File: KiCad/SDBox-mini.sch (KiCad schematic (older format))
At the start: 25 parts, among them J1 DB25_Male, J2 Conn_02x03_Odd_Even, J3 Micro_SD_Card, J4 USB_B_Micro, U1 LM1117-3.3, U2 ATmega328P-AU, U3 74LVC3G17, U4 74LVC1G17, Y1 Crystal_GND24_Small

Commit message: adapted TSSOP-8_3x3mm_P0.65mm footprint for Handsoldering
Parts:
- U3: footprint Package_SO:TSSOP-8_3x3mm_P0.65mm -> SDBox-mini:TSSOP-8_3x3mm_P0.65mm_Custom_Handsoldering
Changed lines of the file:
@@
 F 0 "U3" H 6950 4915 50  0000 C CNN
 F 1 "74LVC3G17" H 6950 4824 50  0000 C CNN
-F 2 "Package_SO:TSSOP-8_3x3mm_P0.65mm" H 7800 4400 50  0001 C CNN
+F 2 "SDBox-mini:TSSOP-8_3x3mm_P0.65mm_Custom_Handsoldering" H 7800 4400 50  0001 C CNN
 F 3 "https://assets.nexperia.com/documents/data-sheet/74LVC3G17.pdf" H 7800 4400 50  0001 C CNN
 	1    6950 4000

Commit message: added optional pull-up on MOSI, fixed keep-out area of copper pour on U3,U4 GND-pads to neighbouring pad
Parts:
- added R6: 10k, Resistor_SMD:R_0603_1608Metric_Pad1.05x0.95mm_HandSolder, symbol Device:R_Small
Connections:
- net +5V: now also R6.2
- net MOSI: now also R6.1
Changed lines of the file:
@@
 Text GLabel 7900 2050 2    50   Input ~ 0
 3V3
-Text GLabel 6550 3450 0    50   Input ~ 0
+Text GLabel 6150 3450 0    50   Input ~ 0
 MOSI
 NoConn ~ 7900 1650
@@
 Wire Wire Line
 	10300 3300 10100 3300
+$Comp
+L Device:R_Small R6
+U 1 1 612033E9
+P 6350 3350
+F 0 "R6" H 6291 3304 50  0000 R CNN
+F 1 "10k" H 6291 3395 50  0000 R CNN
+F 2 "Resistor_SMD:R_0603_1608Metric_Pad1.05x0.95mm_HandSolder" H 6350 3350 50  0001 C CNN
+F 3 "~" H 6350 3350 50  0001 C CNN
+	1    6350 3350
+	-1   0    0    1
+$EndComp
+Text GLabel 6350 3250 1    50   Input ~ 0
+VCC
+Wire Wire Line
+	6350 3450 6550 3450
+Wire Wire Line
+	6150 3450 6350 3450
+Connection ~ 6350 3450
 $EndSCHEMATC

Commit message: added common pull-up for DAT1,DAT2-lines (pin 8 and 1) on MicroSD-connector-pads
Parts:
- added R5: 10k, Resistor_SMD:R_0603_1608Metric_Pad1.05x0.95mm_HandSolder, symbol Device:R_Small
- renumbered R5 to R7
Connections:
- net 3V3: now also R5.2
- net at J3.1 (NC): now also J3.8 (NC), R5.1
- no-connect marks 16 -> 14
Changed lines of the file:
@@
 	3950 1300 4050 1300
 $Comp
-L Device:R_Small R5
+L Device:R_Small R7
 U 1 1 60F84B00
 P 4950 2900
-F 0 "R5" H 4891 2854 50  0000 R CNN
+F 0 "R7" H 4891 2854 50  0000 R CNN
 F 1 "10k" H 4891 2945 50  0000 R CNN
 F 2 "Resistor_SMD:R_0603_1608Metric_Pad1.05x0.95mm_HandSolder" H 4950 2900 50  0001 C CNN
@@
 Text GLabel 4950 3100 2    50   Input ~ 0
 RESET
-NoConn ~ 7900 2350
 Text GLabel 10100 3700 2    50   Output ~ 0
 MISO
@@
 Text GLabel 6150 3450 0    50   Input ~ 0
 MOSI
-NoConn ~ 7900 1650
 Text GLabel 7900 2250 2    50   Input ~ 0
 CS
@@
 	6150 3450 6350 3450
 Connection ~ 6350 3450
+$Comp
+L Device:R_Small R5
+U 1 1 612155E1
+P 8500 1850
+F 0 "R5" H 8441 1804 50  0000 R CNN
+F 1 "10k" H 8441 1895 50  0000 R CNN
+F 2 "Resistor_SMD:R_0603_1608Metric_Pad1.05x0.95mm_HandSolder" H 8500 1850 50  0001 C CNN
+F 3 "~" H 8500 1850 50  0001 C CNN
+	1    8500 1850
+	-1   0    0    1
+$EndComp
+Text GLabel 8500 1750 1    50   Input ~ 0
+3V3
+Wire Wire Line
+	7900 1650 8400 1650
+Wire Wire Line
+	8400 1650 8400 1950
+Wire Wire Line
+	8400 1950 8500 1950
+Wire Wire Line
+	8400 1950 8400 2350
+Wire Wire Line
+	8400 2350 7900 2350
+Connection ~ 8400 1950
 $EndSCHEMATC

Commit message: added a 10k resistor pack and set individual pull-ups for DAT1,DAT2-lines (pin 8,1)
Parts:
- removed R4, R5: 10k, Resistor_SMD:R_0603_1608Metric_Pad1.05x0.95mm_HandSolder, symbol Device:R_Small
- added RN1: 10k, SDBox-mini:RESCAF80P320X160X60-8N, symbol Device:R_Pack04
- renumbered R6 to R4, R7 to R5
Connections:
- net 3V3: now also RN1.5 (R4.2), RN1.6 (R3.2), RN1.7 (R2.2), RN1.8 (R1.2)
- net MISO_3V3: now also RN1.2 (R2.1)
- net DAT1: now reaches J3.8 (NC)
- net DAT1: now also RN1.1 (R1.1); no longer J3.1 (NC)
- new net DAT2: J3.1 (NC), RN1.3 (R3.1)
- no-connect marks 14 -> 15
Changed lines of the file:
@@
 	3950 1300 4050 1300
 $Comp
-L Device:R_Small R7
+L Device:R_Small R5
 U 1 1 60F84B00
 P 4950 2900
-F 0 "R7" H 4891 2854 50  0000 R CNN
+F 0 "R5" H 4891 2854 50  0000 R CNN
 F 1 "10k" H 4891 2945 50  0000 R CNN
 F 2 "Resistor_SMD:R_0603_1608Metric_Pad1.05x0.95mm_HandSolder" H 4950 2900 50  0001 C CNN
@@
 Text GLabel 7550 3250 1    50   Input ~ 0
 GND
-$Comp
-L Device:R_Small R4
-U 1 1 6101E2BD
-P 8950 3400
-F 0 "R4" H 8891 3354 50  0000 R CNN
-F 1 "10k" H 8891 3445 50  0000 R CNN
-F 2 "Resistor_SMD:R_0603_1608Metric_Pad1.05x0.95mm_HandSolder" H 8950 3400 50  0001 C CNN
-F 3 "~" H 8950 3400 50  0001 C CNN
-	1    8950 3400
-	-1   0    0    1
-$EndComp
-Text GLabel 8950 3300 1    50   Input ~ 0
-3V3
 Text GLabel 7900 2150 2    50   Input ~ 0
 MOSI_3V3
@@
 Text GLabel 7900 1750 2    50   Output ~ 0
 MISO_3V3
-Text GLabel 8850 3500 0    50   Input ~ 0
+Text GLabel 9200 3500 0    50   Input ~ 0
 MISO_3V3
-Wire Wire Line
-	8850 3500 8950 3500
 Text GLabel 6550 3800 0    50   Output ~ 0
 SCK_3V3
@@
 Text GLabel 10600 3300 2    50   Input ~ 0
 VCC
-Wire Wire Line
-	8950 3500 9200 3500
-Connection ~ 8950 3500
 Text GLabel 9200 3700 0    50   Input ~ 0
 GND
@@
 	10300 3300 10100 3300
 $Comp
-L Device:R_Small R6
+L Device:R_Small R4
 U 1 1 612033E9
 P 6350 3350
-F 0 "R6" H 6291 3304 50  0000 R CNN
+F 0 "R4" H 6291 3304 50  0000 R CNN
 F 1 "10k" H 6291 3395 50  0000 R CNN
 F 2 "Resistor_SMD:R_0603_1608Metric_Pad1.05x0.95mm_HandSolder" H 6350 3350 50  0001 C CNN
@@
 	6150 3450 6350 3450
 Connection ~ 6350 3450
-$Comp
-L Device:R_Small R5
-U 1 1 612155E1
-P 8500 1850
-F 0 "R5" H 8441 1804 50  0000 R CNN
-F 1 "10k" H 8441 1895 50  0000 R CNN
-F 2 "Resistor_SMD:R_0603_1608Metric_Pad1.05x0.95mm_HandSolder" H 8500 1850 50  0001 C CNN
-F 3 "~" H 8500 1850 50  0001 C CNN
-	1    8500 1850
-	-1   0    0    1
-$EndComp
-Text GLabel 8500 1750 1    50   Input ~ 0
+Text GLabel 8250 1050 1    50   Input ~ 0
 3V3
-Wire Wire Line
-	7900 1650 8400 1650
-Wire Wire Line
-	8400 1650 8400 1950
-Wire Wire Line
-	8400 1950 8500 1950
-Wire Wire Line
-	8400 1950 8400 2350
-Wire Wire Line
-	8400 2350 7900 2350
-Connection ~ 8400 1950
+$Comp
+L Device:R_Pack04 RN1
+U 1 1 6124C116
+P 8600 1250
+F 0 "RN1" H 8788 1296 50  0000 L CNN
+F 1 "10k" H 8788 1205 50  0000 L CNN
+F 2 "SDBox-mini:RESCAF80P320X160X60-8N" V 8875 1250 50  0001 C CNN
+F 3 "~" H 8600 1250 50  0001 C CNN
+	1    8600 1250
+	1    0    0    -1
+$EndComp
+Text GLabel 7900 1650 2    50   Input ~ 0
+DAT1
+Text GLabel 7900 2350 2    50   Input ~ 0
+DAT2
+Text GLabel 8400 1450 3    50   Input ~ 0
+DAT1
+Text GLabel 8600 1450 3    50   Input ~ 0
+DAT2
+Text GLabel 8500 1450 3    50   Input ~ 0
+MISO_3V3
+Wire Wire Line
+	8400 1050 8500 1050
+Connection ~ 8500 1050
+Wire Wire Line
+	8500 1050 8600 1050
+NoConn ~ 8700 1450
+Wire Wire Line
+	8600 1050 8700 1050
+Connection ~ 8600 1050
+Wire Wire Line
+	8250 1050 8400 1050
+Connection ~ 8400 1050
 $EndSCHEMATC

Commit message: cleanup of lib symbols and pcb silkscreen text
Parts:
- J3: value Micro_SD_Card -> Micro_SD_Card_Socket; symbol SDBox-mini:Micro_SD_Card -> SDBox-mini:Micro_SD_Card_Socket
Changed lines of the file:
@@
 	9550 2050 9950 2050
 $Comp
-L SDBox-mini:Micro_SD_Card J3
+L SDBox-mini:Micro_SD_Card_Socket J3
 U 1 1 610B5617
 P 7000 2050
 F 0 "J3" H 6950 1233 50  0000 C CNN
-F 1 "Micro_SD_Card" H 6950 1324 50  0000 C CNN
+F 1 "Micro_SD_Card_Socket" H 6950 1324 50  0000 C CNN
 F 2 "SDBox-mini:GCT-MEM2055-00-190-01-A" H 8150 2350 50  0001 C CNN
 F 3 "" H 7000 2050 50  0001 C CNN

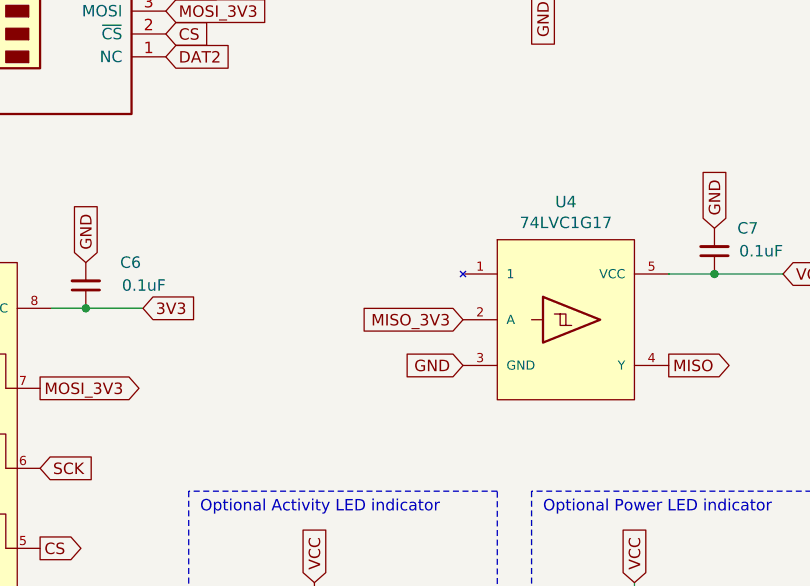
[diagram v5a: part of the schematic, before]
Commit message: Replaced U4 (74LVC1G17) with 74AHCT1G126 (same footprint), added pull-up resistor with 2.0mm two-pin-jumper for tristate MISO high-Z when flashing new fw
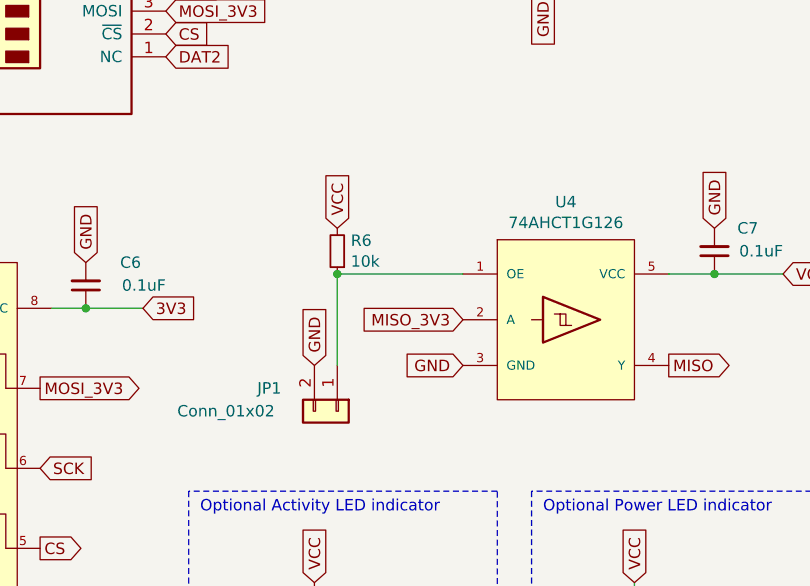
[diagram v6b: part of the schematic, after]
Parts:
- removed U4: 74LVC1G17, SDBox-mini:SOT-353_SC-70-5_Custom_Handsoldering, symbol SDBox-mini:74LVC1G17
- added JP1: Conn_01x02, Connector_PinHeader_2.00mm:PinHeader_1x02_P2.00mm_Vertical, symbol Connector_Generic:Conn_01x02
- added R6: 10k, Resistor_SMD:R_0603_1608Metric_Pad1.05x0.95mm_HandSolder, symbol Device:R_Small
- added U4: 74AHCT1G126, SDBox-mini:SOT-353_SC-70-5_Custom_Handsoldering, symbol SDBox-mini:74AHCT1G126
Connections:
- net +5V: now also R6.2, U4.5 (VCC)
- net GND: now also JP1.2 (Pin_2), U4.3 (GND)
- net MISO: now also U4.4 (Y)
- net MISO_3V3: now also U4.2 (A)
- new net: JP1.1 (Pin_1), R6.1, U4.1 (OE)
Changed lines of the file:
@@
 Wire Wire Line
 	6050 4150 6550 4150
-$Comp
-L SDBox-mini:74LVC1G17 U4
-U 1 1 611C568A
-P 9650 3500
-F 0 "U4" H 9650 4015 50  0000 C CNN
-F 1 "74LVC1G17" H 9650 3924 50  0000 C CNN
-F 2 "SDBox-mini:SOT-353_SC-70-5_Custom_Handsoldering" H 10150 4450 50  0001 C CNN
-F 3 "https://www.ti.com/lit/ds/symlink/sn74lvc1g17-q1.pdf" H 10150 4450 50  0001 C CNN
-	1    9650 3500
-	1    0    0    -1
-$EndComp
 Connection ~ 10300 3300
 Wire Wire Line
@@
 	8250 1050 8400 1050
 Connection ~ 8400 1050
+$Comp
+L SDBox-mini:74AHCT1G126 U4
+U 1 1 6297BF16
+P 9650 3500
+F 0 "U4" H 9650 4015 50  0000 C CNN
+F 1 "74AHCT1G126" H 9650 3924 50  0000 C CNN
+F 2 "SDBox-mini:SOT-353_SC-70-5_Custom_Handsoldering" H 10150 4450 50  0001 C CNN
+F 3 "https://www.diodes.com/assets/Datasheets/74AHCT1G126.pdf" H 10150 4450 50  0001 C CNN
+	1    9650 3500
+	1    0    0    -1
+$EndComp
+$Comp
+L Connector_Generic:Conn_01x02 JP1
+U 1 1 62981047
+P 8650 3900
+F 0 "JP1" V 8550 3550 50  0000 L CNN
+F 1 "Conn_01x02" V 8650 3200 50  0000 L CNN
+F 2 "Connector_PinHeader_2.00mm:PinHeader_1x02_P2.00mm_Vertical" H 8650 3900 50  0001 C CNN
+F 3 "~" H 8650 3900 50  0001 C CNN
+	1    8650 3900
+	0    1    1    0
+$EndComp
+Text GLabel 8550 3700 1    50   Input ~ 0
+GND
+$Comp
+L Device:R_Small R6
+U 1 1 62986CE1
+P 8650 3200
+F 0 "R6" H 8591 3154 50  0000 R CNN
+F 1 "10k" H 8591 3245 50  0000 R CNN
+F 2 "Resistor_SMD:R_0603_1608Metric_Pad1.05x0.95mm_HandSolder" H 8650 3200 50  0001 C CNN
+F 3 "~" H 8650 3200 50  0001 C CNN
+	1    8650 3200
+	-1   0    0    1
+$EndComp
+Text GLabel 8650 3100 1    50   Input ~ 0
+VCC
+Wire Wire Line
+	9200 3300 8650 3300
+Wire Wire Line
+	8650 3700 8650 3300
+Connection ~ 8650 3300
 $EndSCHEMATC
